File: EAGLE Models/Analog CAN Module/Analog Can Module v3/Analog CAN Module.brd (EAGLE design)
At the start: 98.3 x 80 mm, 241 parts, among them IC1 AT90CAN128, IC2 MCP2551SO8, IC3 NUP2105L, IC5 FT232RL, Q1 56P2859, U1 LTC2053, U10 LTC2053, U11 LTC2053, U12 LTC2053, U13 LTC2053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

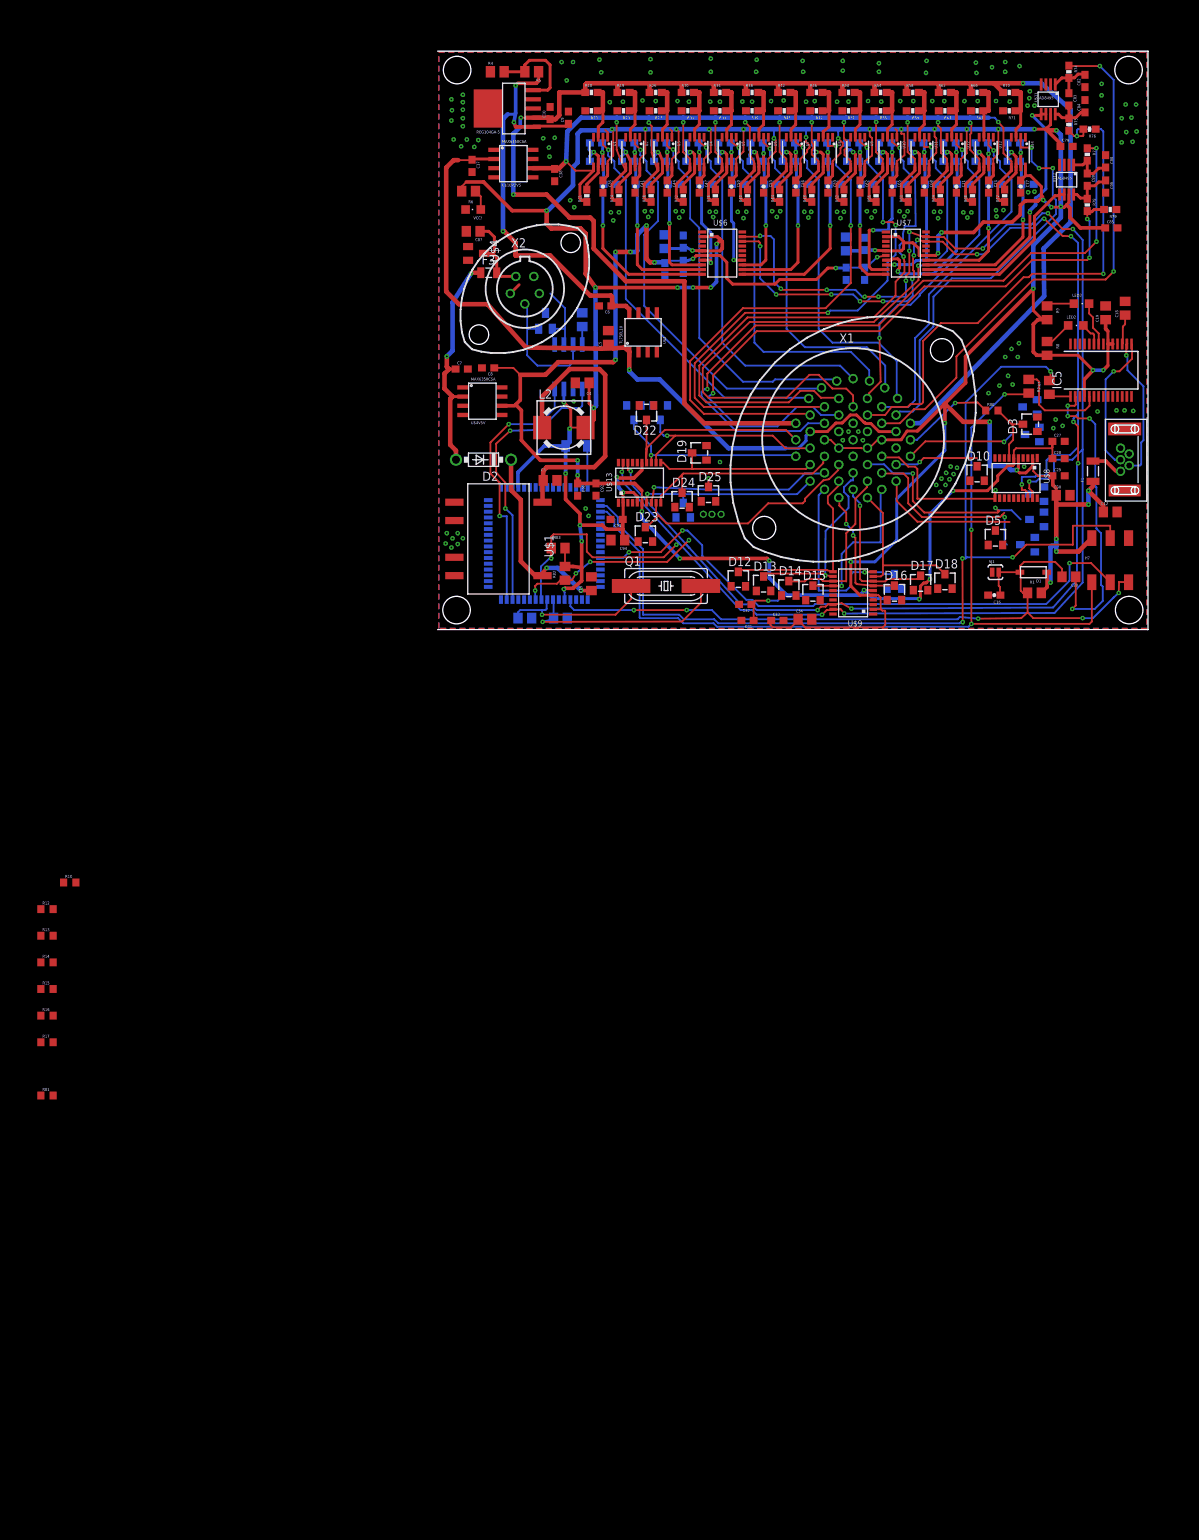
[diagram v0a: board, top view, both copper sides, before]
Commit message: Added CC resistors
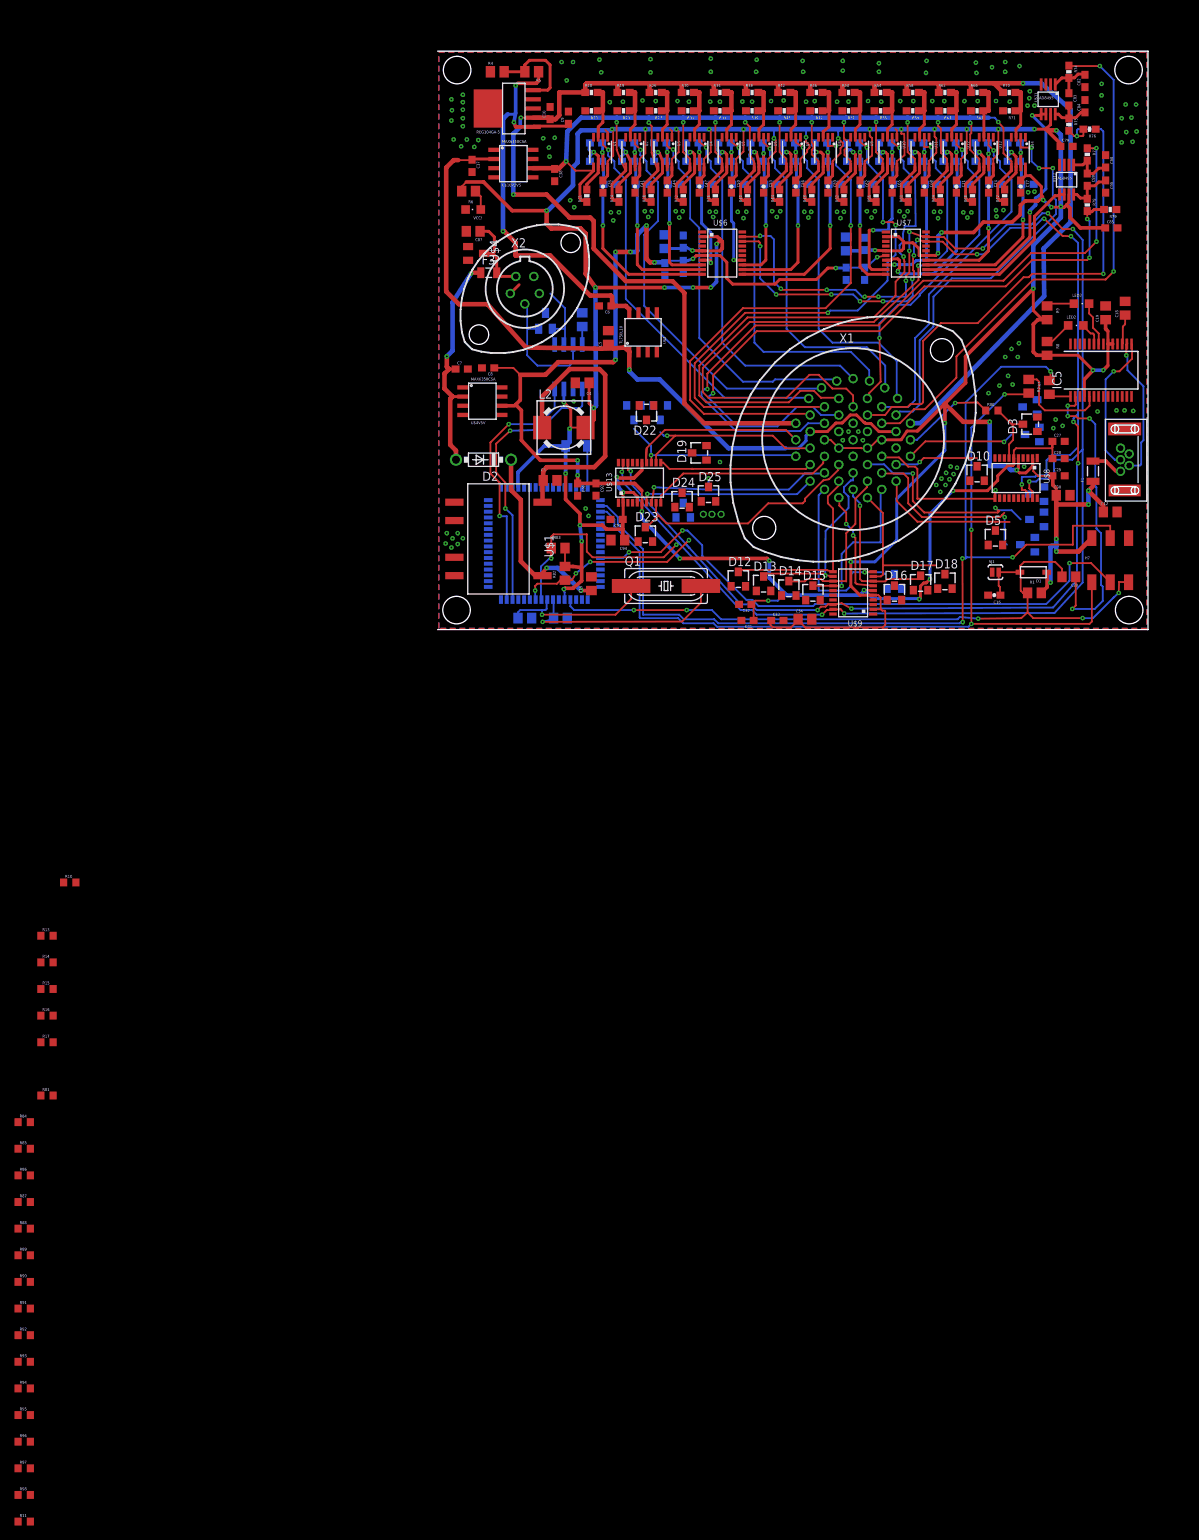
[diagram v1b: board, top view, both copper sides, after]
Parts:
- removed R12: (no value), rcl:R0603
- added R11, R84, R85, R86, R87, R88, R89, R90, R91, R92, R93, R94, R95, R96, R97, R98: (no value), rcl:R0603
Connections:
- new net A10CC: D17.C, R90.2
- new net A11CC: D18.C, R88.2
- new net A12CC: D11.C, R11.2
- new net A13CC: D12.C, R84.2
- new net A14CC: D13.C, R85.2
- new net A15CC: D14.C, R86.2
- new net A16CC: D15.C, R87.2
- new net A17CC: D26.C, R91.2
- new net A18CC: D25.C, R92.2
- new net A19CC: D23.C, R93.2
- new net A20CC: D24.C, R94.2
- new net A21CC: D19.C, R98.2
- new net A22CC: D20.C, R97.2
- new net A23CC: D21.C, R96.2
- new net A24CC: D22.C, R95.2
- new net A9CC: D16.C, R89.2
- net A10: now also R90.1; no longer D17.C
- net A11: now also R88.1; no longer D18.C
- net A12: now also R11.1; no longer D11.C
- net A13: now also R84.1; no longer D12.C
- net A14: now also R85.1; no longer D13.C
- net A15: now also R86.1; no longer D14.C
- net A16: now also R87.1; no longer D15.C
- net A17: now also R91.1; no longer D26.C
- net A18: now also R92.1; no longer D25.C
- net A19: now also R93.1; no longer D23.C
- net A20: now also R94.1; no longer D24.C
- net A21: now also R98.1; no longer D19.C
- net A22: now also R97.1; no longer D20.C
- net A23: now also R96.1; no longer D21.C
- net A24: now also R95.1; no longer D22.C
- net A8: no longer R12.1
- net A8CC: no longer R12.2
- net A9: now also R89.1; no longer D16.C
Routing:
- net A24: track 29.9 -> 25.9 mm
- net A9: track 18.2 -> 15.3 mm
- net A20: track 28.8 -> 26.3 mm
- net A21: track 23.5 -> 21.3 mm
- net A11: track 22.1 -> 20.4 mm
- net A22: track 28.2 -> 26.5 mm
- net A12: track 28.1 -> 26.8 mm
- net A23: track 27.0 -> 25.8 mm
- net A17: track 25.8 -> 24.5 mm
- net A18: track 29.4 -> 28.3 mm
- net SG5V: track 228.4 -> 227.4 mm
- net A10: track 21.6 -> 21.0 mm
- net A14: track 26.4 -> 25.9 mm

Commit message: expanded board and added resistors to left ADC
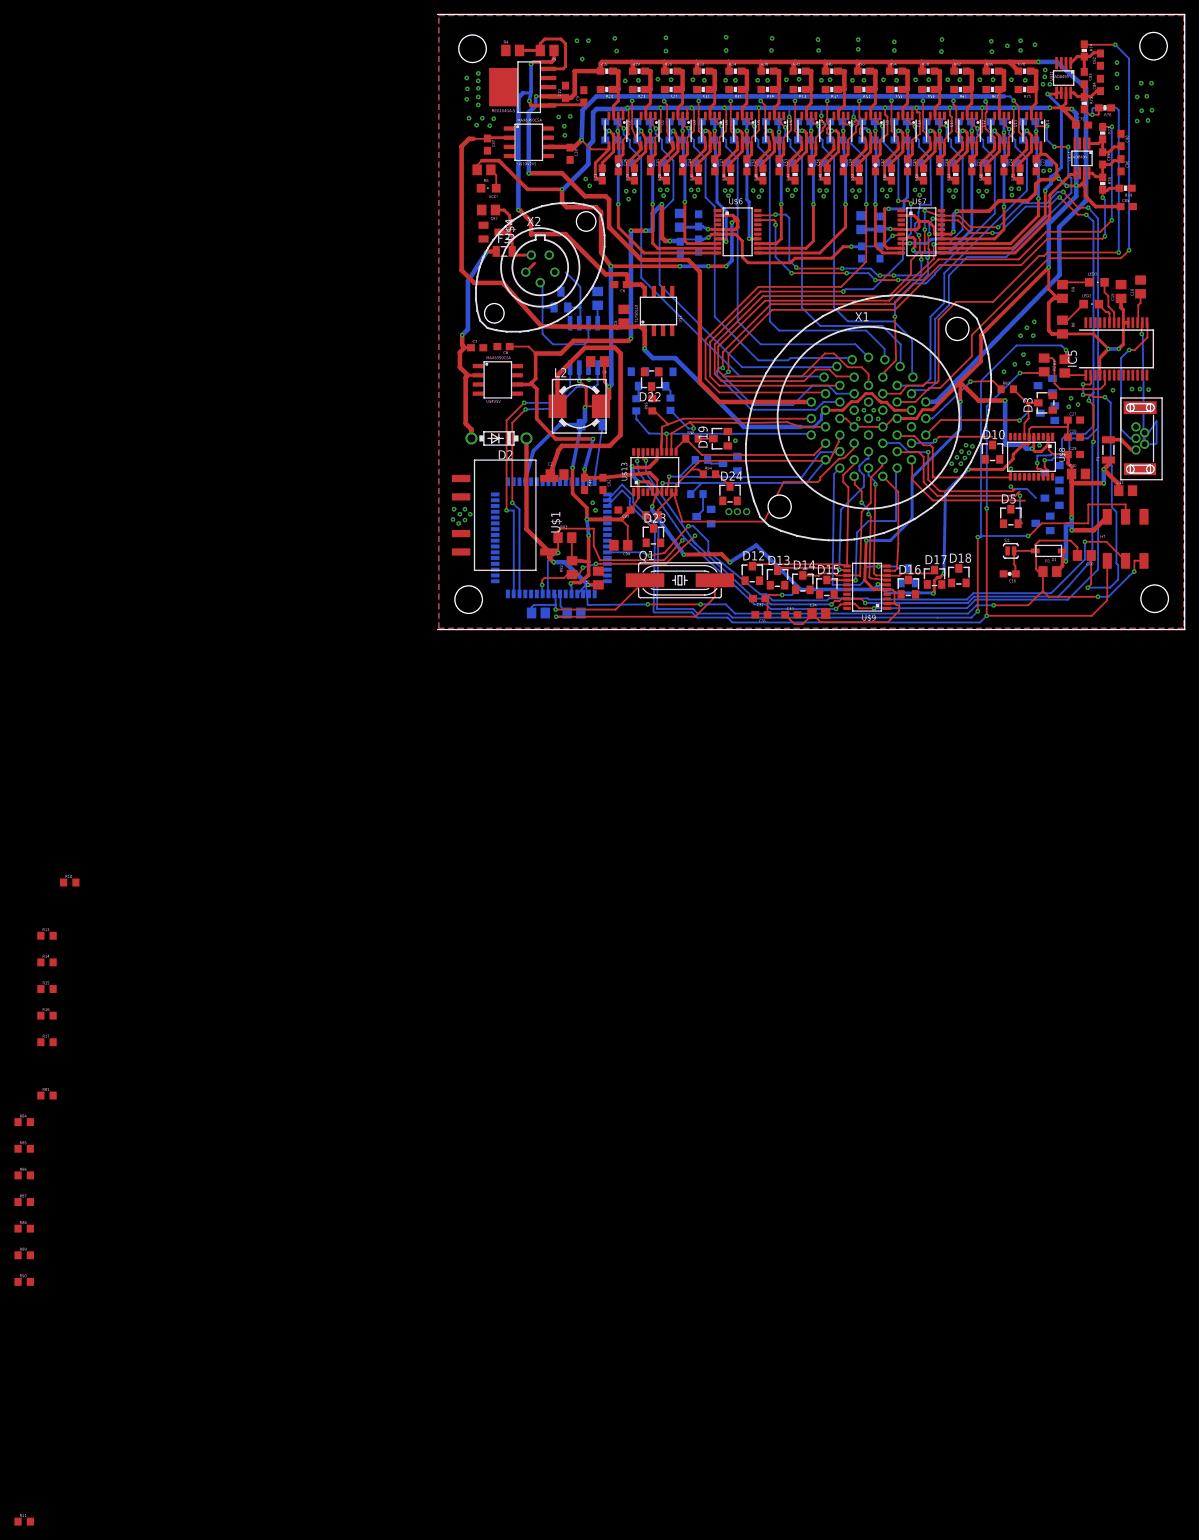
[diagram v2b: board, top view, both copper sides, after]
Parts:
- moved R98 172.8 mm to (35.2, 26.4)
- moved R97 172.2 mm to (32.2, 31.2), flipped to the bottom, turned to 90 degrees
- moved R96 166.5 mm to (27.5, 31.1), flipped to the bottom, turned to 90 degrees
- moved R95 164.5 mm to (29.7, 31.1), turned to 90 degrees
- moved R94 158.0 mm to (37.6, 21.5)
- moved R92 153.1 mm to (36.5, 23.5), flipped to the bottom, turned to 180 degrees
- moved R91 146.1 mm to (35.9, 18.7), flipped to the bottom, turned to 180 degrees
- moved R93 145.8 mm to (29.7, 15.8), turned to 180 degrees
- moved D24 6.69 mm to (40.4, 18.8)
- moved D25 5.19 mm to (40.5, 23.0), flipped to the bottom, turned to 270 degrees
- moved D21 4.72 mm to (27.8, 34.7)
- moved D20 4.71 mm to (31.6, 34.7)
- moved D22 4.68 mm to (29.6, 34.6)
- moved C79 3.64 mm to (89.1, 69.8)
- moved C82 3.64 mm to (91.7, 78.8)
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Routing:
- net VCC: track 649.6 -> 658.2 mm
- net 5VREF: track 211.9 -> 220.1 mm
- net TX: track 123.3 -> 130.6 mm
- net RX: track 134.2 -> 140.3 mm
- net A11: track 20.4 -> 15.2 mm
- net A19: track 33.5 -> 38.3 mm
- net D-: track 19.6 -> 24.4 mm
- net A24: track 25.9 -> 30.4 mm
- net RESET: track 103.5 -> 107.4 mm
- net SCL: track 235.1 -> 238.6 mm
- net A17CC: track 0.00 -> 3.48 mm
- net A22: track 26.5 -> 29.8 mm
- net A20: track 26.3 -> 29.4 mm
- net A23: track 25.8 -> 28.8 mm
- net A17: track 24.5 -> 27.5 mm
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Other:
- board size 98.3 x 80 mm -> 103.3 x 85.1 mm

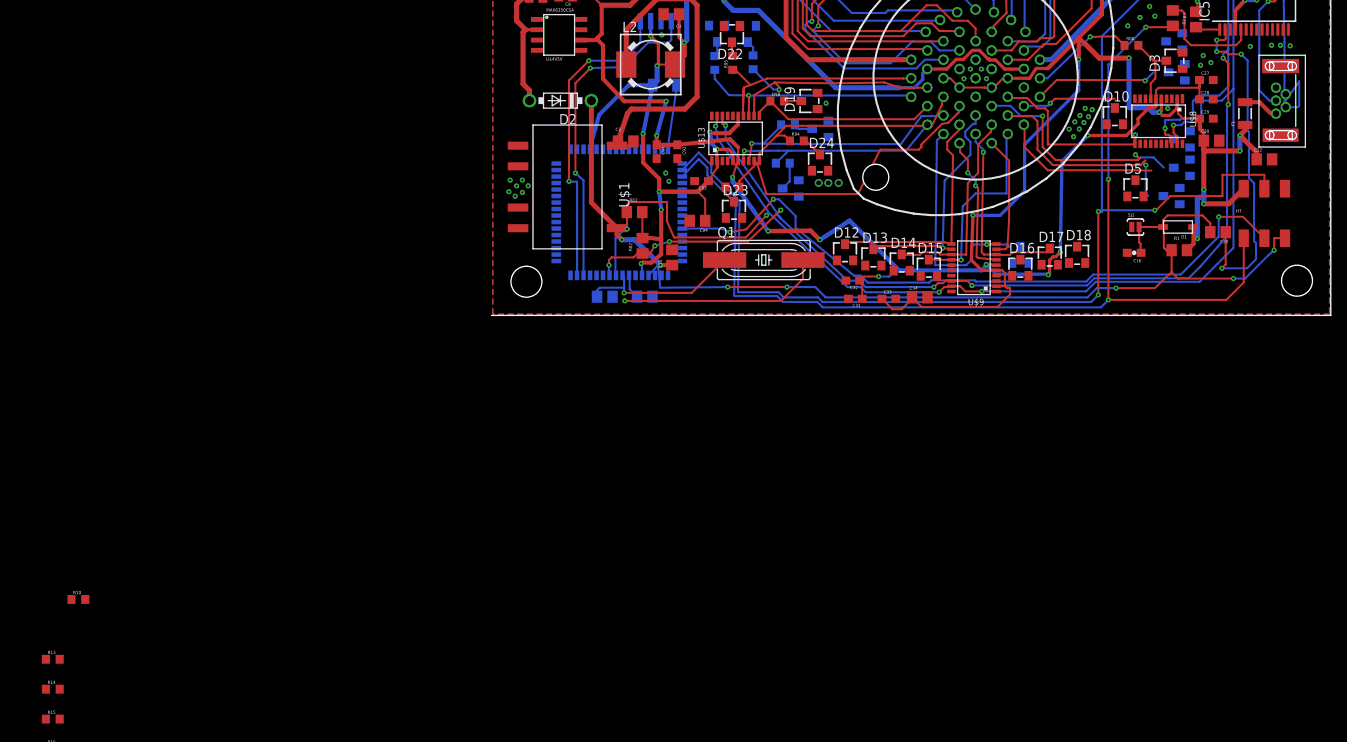
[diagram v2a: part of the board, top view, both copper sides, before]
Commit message: added GLV+ connector and added resistors to ADC
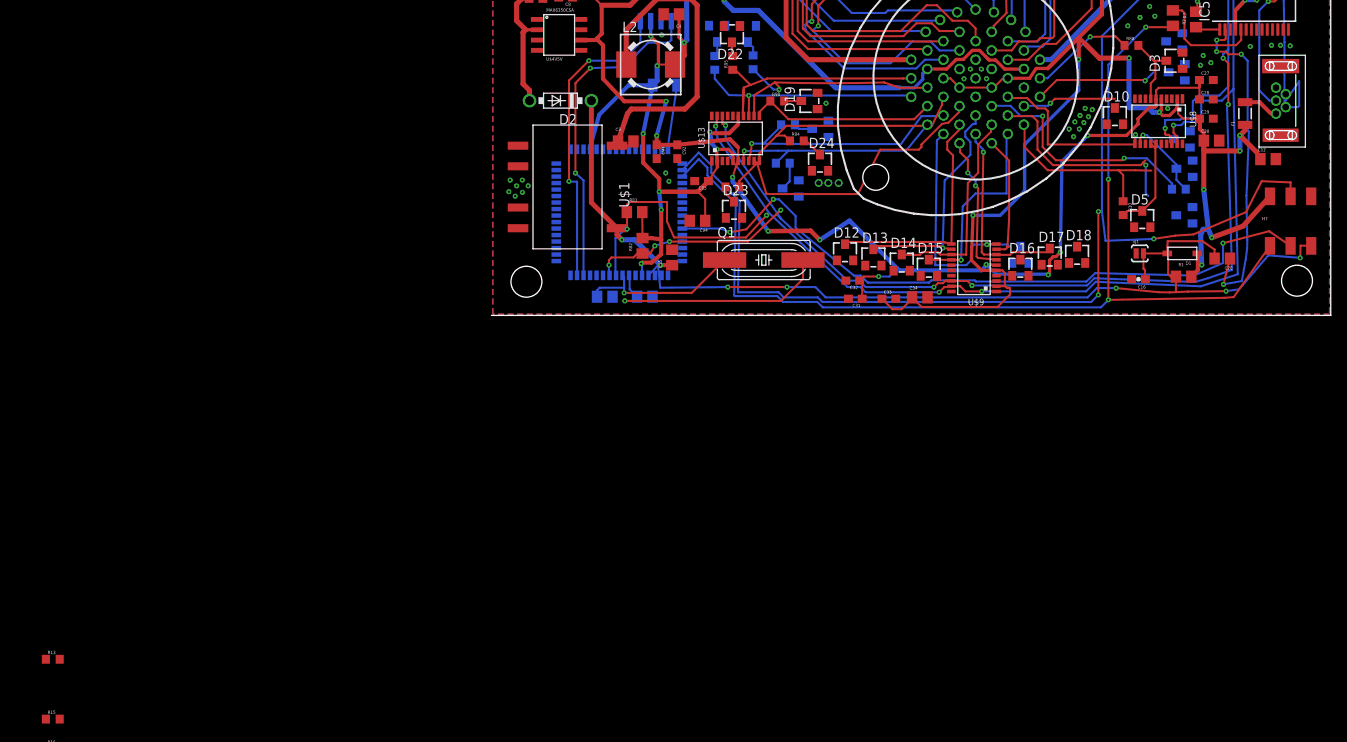
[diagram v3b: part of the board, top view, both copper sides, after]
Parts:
- moved R14 151.7 mm to (84.6, 15.5), flipped to the bottom, turned to 180 degrees
- moved R10 137.4 mm to (77.8, 13.2), turned to 270 degrees
- moved D5 3.88 mm to (80.1, 11.9)
- moved H7 3.36 mm to (98.4, 11.6)
- moved C20 3.29 mm to (90.0, 7.00)
- moved D1 3.29 mm to (85.1, 7.63)
- moved R1 3.29 mm to (85.2, 4.78)
- moved SJ1 3.29 mm to (79.8, 7.63)
- moved C16 3.29 mm to (79.7, 4.46)
- moved D6 2.84 mm to (85.3, 12.3)
- moved C12 0.46 mm to (95.6, 19.2)
- moved D7 0.35 mm to (85.3, 18.1)
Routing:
- net A8CC: track 0.00 -> 11.7 mm
- net A6CC: track 0.00 -> 10.3 mm, vias 0 -> 1
- net VCC: track 658.2 -> 665.2 mm
- net RX: track 140.3 -> 146.2 mm
- net A8: track 19.6 -> 23.6 mm
- net SDA: track 234.3 -> 237.0 mm
- net SCL: track 238.6 -> 241.0 mm
- net RESET: track 107.4 -> 109.6 mm
- net DTR: track 42.2 -> 40.9 mm
- net AVR_SCK: track 84.2 -> 85.5 mm
- net A6: track 28.2 -> 29.3 mm
